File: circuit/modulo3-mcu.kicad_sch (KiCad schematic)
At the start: 46 parts, among them Q1 BS250, Q2 BS170, U1 74LVC2G32DC, U10 PWR_CONN, U11 FOOTSWITCH, U2 AVR64DA64, U3 SN74LVC1G17, U4 UPDI, U5 TOUCHSCREEN_240x320, U6 FV1_CONN, U7 DBG_UART, U8 AMPCTRL, Y1 32768Hz

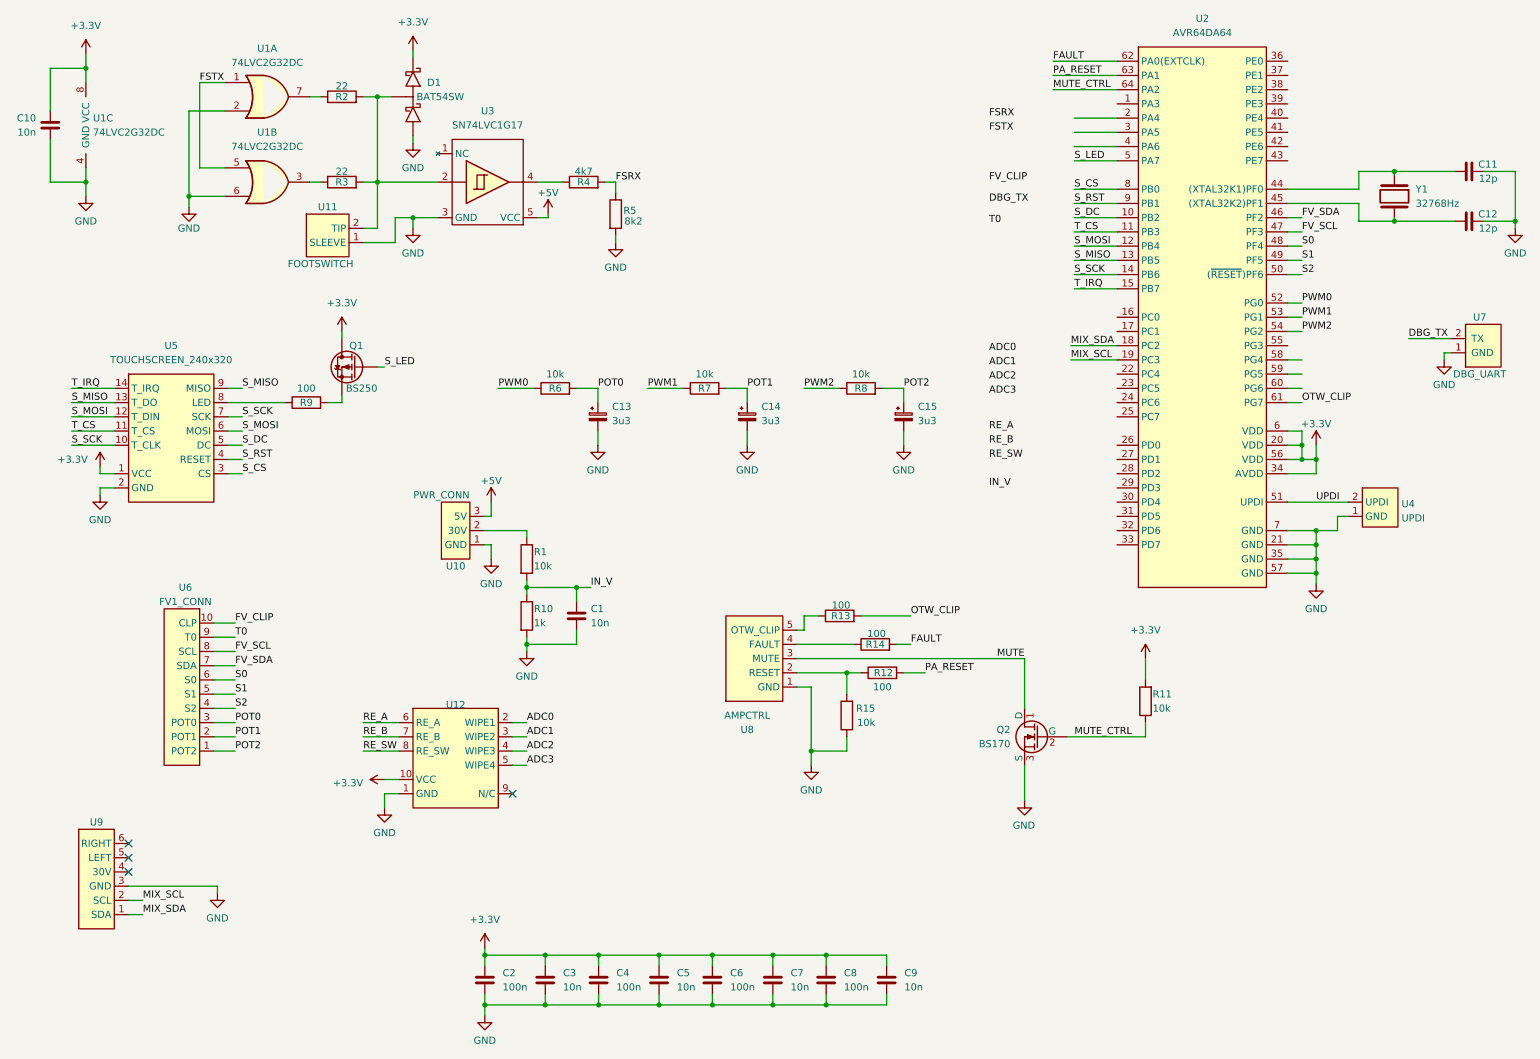
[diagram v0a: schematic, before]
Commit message: mcu pcb first draft done!
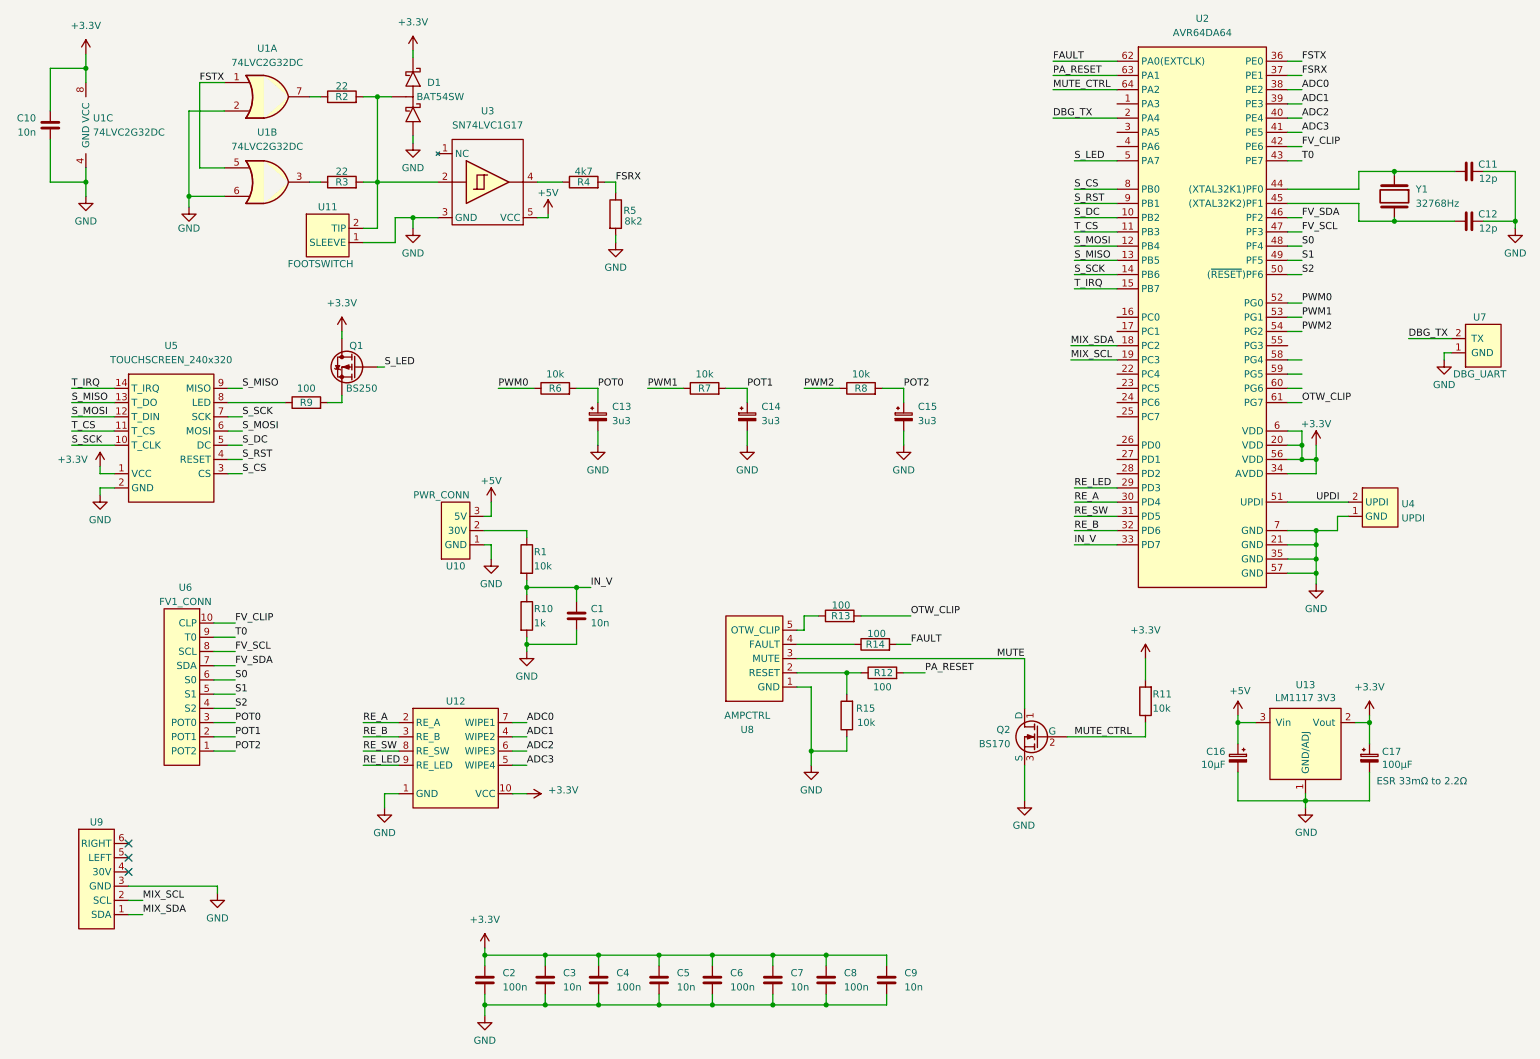
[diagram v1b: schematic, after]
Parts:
- added C16: 10µF, myAmp:CPOL_D4_P1.5, symbol myAmp:CPOL
- added C17: 100µF, myAmp:CPOL_D6.3_P2.5, symbol myAmp:CPOL
- added U13: LM1117 3V3, myAmp:SOT-223, symbol myAmp:LM1117
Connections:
- net +3.3V: now also C17.1, U13.2 (Vout)
- net +5V: now also C16.1, U13.3 (Vin)
- net ADC0: now also U12.7 (WIPE1), U2.38 (PE2); no longer U12.2 (WIPE1)
- net ADC1: now also U12.4 (WIPE2), U2.39 (PE3); no longer U12.3 (WIPE2)
- net ADC2: now also U12.6 (WIPE3), U2.40 (PE4); no longer U12.4 (WIPE3)
- net ADC3: now also U2.41 (PE5)
- net DBG_TX: now also U2.2 (PA4)
- net FSRX: now also U2.37 (PE1)
- net FSTX: now also U2.36 (PE0)
- net FV_CLIP: now also U2.42 (PE6)
- net GND: now also C16.2, C17.2, U13.1 (GND/ADJ)
- net IN_V: now also U2.33 (PD7)
- net RE_A: now also U12.2 (RE_A), U2.30 (PD4); no longer U12.6 (RE_A)
- net RE_B: now also U12.3 (RE_B), U2.32 (PD6); no longer U12.7 (RE_B)
- net RE_SW: now also U2.31 (PD5)
- net T0: now also U2.43 (PE7)
- net RE_LED: now reaches U2.29 (PD3)
- net RE_LED: now also U12.9 (RE_LED)
- no-connect marks 4 -> 3
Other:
- note added: "ESR 33mΩ to 2.2Ω"

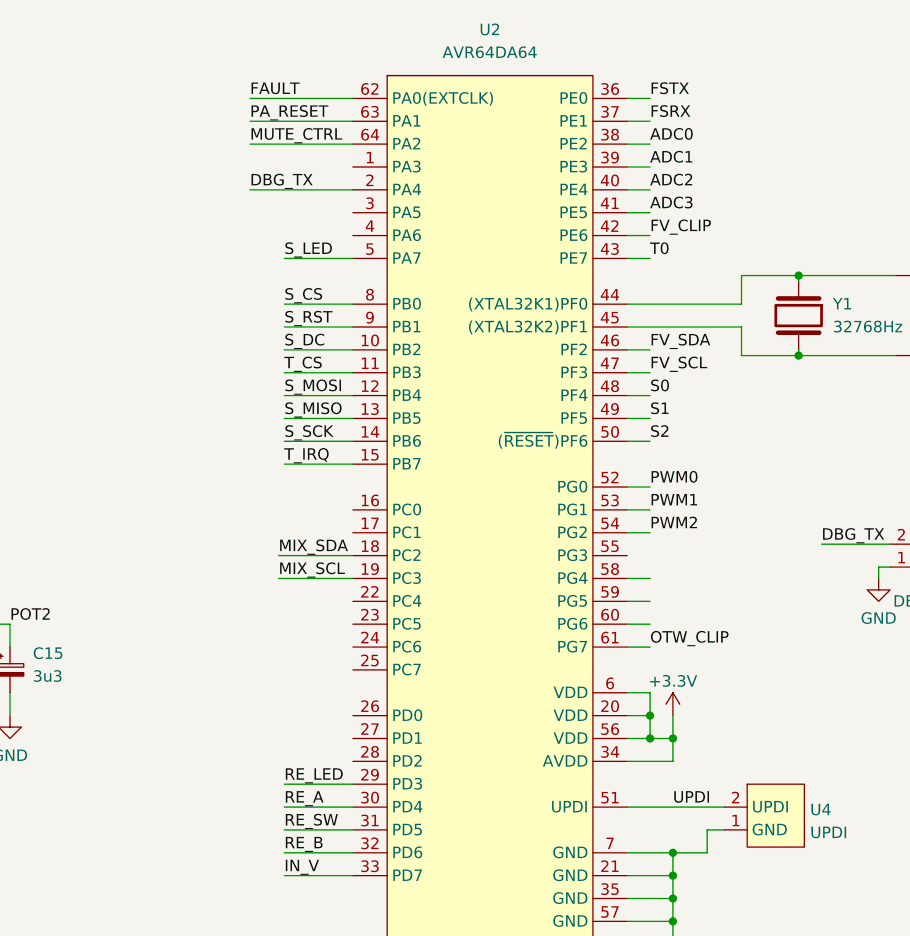
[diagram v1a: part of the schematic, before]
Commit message: added test pads for unused mcu pins
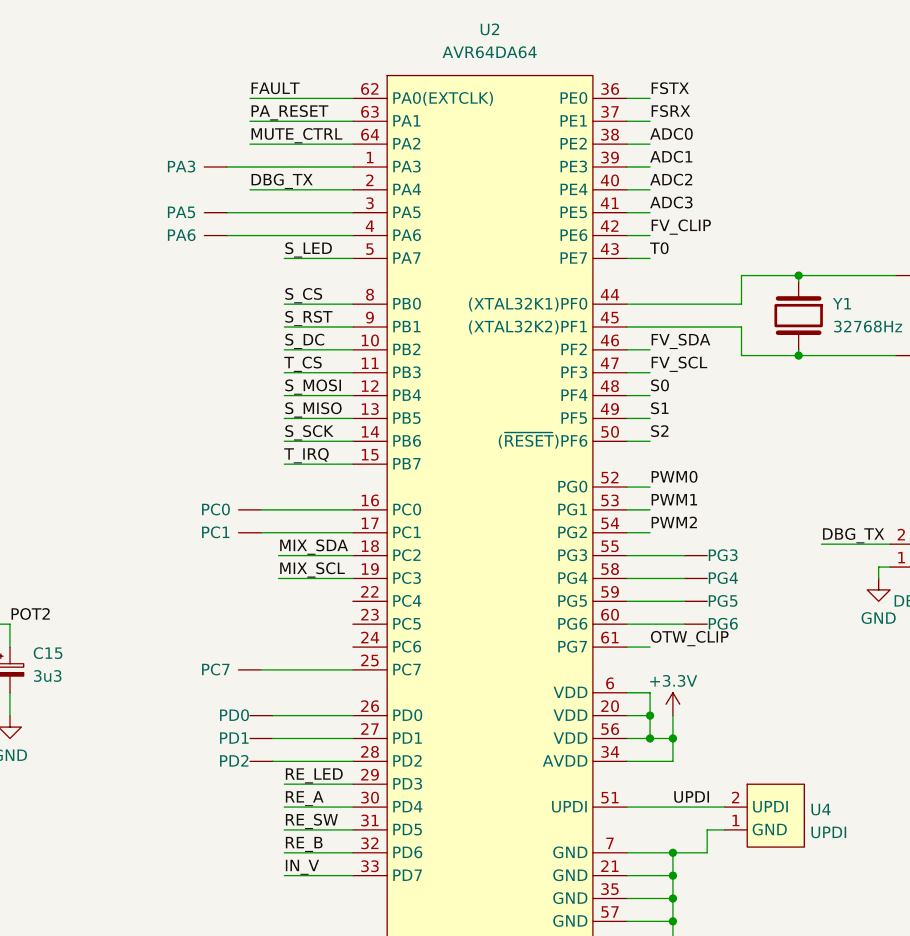
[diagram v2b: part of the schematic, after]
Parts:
- added T1: PA3, myAmp:TestPad, symbol myAmp:TEST
- added T10: PD1, myAmp:TestPad, symbol myAmp:TEST
- added T11: PD0, myAmp:TestPad, symbol myAmp:TEST
- added T12: PC7, myAmp:TestPad, symbol myAmp:TEST
- added T13: PG6, myAmp:TestPad, symbol myAmp:TEST
- added T2: PD2, myAmp:TestPad, symbol myAmp:TEST
- added T3: PA6, myAmp:TestPad, symbol myAmp:TEST
- added T4: PC0, myAmp:TestPad, symbol myAmp:TEST
- added T5: PC1, myAmp:TestPad, symbol myAmp:TEST
- added T6: PG5, myAmp:TestPad, symbol myAmp:TEST
- added T7: PG4, myAmp:TestPad, symbol myAmp:TEST
- added T8: PG3, myAmp:TestPad, symbol myAmp:TEST
- added T9: PA5, myAmp:TestPad, symbol myAmp:TEST
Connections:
- net at U2.1 (PA3): now also T1.1
- net at U2.16 (PC0): now also T4.1
- net at U2.17 (PC1): now also T5.1
- net at U2.25 (PC7): now also T12.1
- net at U2.26 (PD0): now also T11.1
- net at U2.27 (PD1): now also T10.1
- net at U2.28 (PD2): now also T2.1
- net at U2.3 (PA5): now also T9.1
- net at U2.4 (PA6): now also T3.1
- net at U2.55 (PG3): now also T8.1
- net at U2.58 (PG4): now also T7.1
- net at U2.59 (PG5): now also T6.1
- net at U2.60 (PG6): now also T13.1

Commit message: ready to panelize
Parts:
- removed U11: FOOTSWITCH, myAmp:FOOTSWITCH, symbol myAmp:FOOTSWITCH
- added T14: PC4, myAmp:TestPad, symbol myAmp:TEST
- added T15: PC5, myAmp:TestPad, symbol myAmp:TEST
- added T16: PC6, myAmp:TestPad, symbol myAmp:TEST
- added U11: FOOTSWITCH, myAmp:EXT_JACK, symbol myAmp:EXT_JACK
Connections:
- net GND: now also U11.1 (SLEEVE)
- net at D1.3, R2.2, R3.2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: now also U11.2 (TIP)
- net at U2.22 (PC4): now also T14.1
- net at U2.23 (PC5): now also T15.1
- net at U2.24 (PC6): now also T16.1
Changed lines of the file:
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@@
     (stroke (width 0) (type default))
   )
+  (wire (pts (xy 200.66 80.01) (xy 210.82 80.01))
+    (stroke (width 0) (type default))
+  )
   (wire (pts (xy 52.07 85.09) (xy 54.61 85.09))
     (stroke (width 0) (type default))
@@
     (stroke (width 0) (type default))
   )
+  (wire (pts (xy 200.66 82.55) (xy 210.82 82.55))
+    (stroke (width 0) (type default))
+  )
   (wire (pts (xy 97.917 188.214) (xy 97.917 190.119))
     (stroke (width 0) (type default))
@@
     (stroke (width 0) (type default))
   )
+  (wire (pts (xy 200.66 77.47) (xy 210.82 77.47))
+    (stroke (width 0) (type default))
+  )
   (wire (pts (xy 262.89 71.12) (xy 270.51 71.12))
     (stroke (width 0) (type default))
@@
     )
   )
-  (symbol (lib_id "myAmp:FOOTSWITCH") (at 71.12 52.705 0) (unit 1)
-    (in_bom yes) (on_board yes) (dnp no)
-    (property "Reference" "U11" (at 69.85 47.625 0)
-      (effects (font (size 1.27 1.27)))
-    )
-    (property "Value" "FOOTSWITCH" (at 68.58 57.785 0)
-      (effects (font (size 1.27 1.27)))
-    )
-    (property "Footprint" "myAmp:FOOTSWITCH" (at 76.2 52.705 0)
-      (effects (font (size 1.27 1.27)) hide)
-    )
-    (property "Datasheet" "" (at 76.2 52.705 0)
-      (effects (font (size 1.27 1.27)) hide)
-    )
-    (pin "1")
-    (pin "2")
-    (instances
-      (project "modulo3-mcu"
-        (path "/0f0bc50f-3b2c-45bf-9734-4d8155cef241"
-          (reference "U11") (unit 1)
-        )
-      )
-    )
-  )
   (symbol (lib_id "myAmp:R") (at 137.16 80.01 90) (unit 1)
     (in_bom yes) (on_board yes) (dnp no)
@@
     )
   )
+  (symbol (lib_id "myAmp:EXT_JACK") (at 71.12 52.705 0) (unit 1)
+    (in_bom yes) (on_board yes) (dnp no)
+    (property "Reference" "U11" (at 69.85 47.625 0)
+      (effects (font (size 1.27 1.27)))
+    )
+    (property "Value" "FOOTSWITCH" (at 69.85 57.785 0)
+      (effects (font (size 1.27 1.27)))
+    )
+    (property "Footprint" "myAmp:EXT_JACK" (at 71.12 57.785 0)
+      (effects (font (size 1.27 1.27)) hide)
+    )
+    (property "Datasheet" "" (at 76.2 52.705 0)
+      (effects (font (size 1.27 1.27)) hide)
+    )
+    (pin "1")
+    (pin "2")
+    (instances
+      (project "modulo3-mcu"
+        (path "/0f0bc50f-3b2c-45bf-9734-4d8155cef241"
+          (reference "U11") (unit 1)
+        )
+      )
+    )
+  )
   (symbol (lib_id "power:+3.3V") (at 72.39 69.85 0) (unit 1)
     (in_bom yes) (on_board yes) (dnp no) (fields_autoplaced)
@@
     )
   )
+  (symbol (lib_id "myAmp:TEST") (at 198.12 82.55 180) (unit 1)
+    (in_bom yes) (on_board yes) (dnp no)
+    (property "Reference" "T16" (at 198.12 78.74 0)
+      (effects (font (size 1.27 1.27)) hide)
+    )
+    (property "Value" "PC6" (at 195.58 82.55 0)
+      (effects (font (size 1.27 1.27)))
+    )
+    (property "Footprint" "myAmp:TestPad" (at 198.12 82.55 0)
+      (effects (font (size 1.27 1.27)) hide)
+    )
+    (property "Datasheet" "" (at 198.12 82.55 0)
+      (effects (font (size 1.27 1.27)) hide)
+    )
+    (pin "1")
+    (instances
+      (project "modulo3-mcu"
+        (path "/0f0bc50f-3b2c-45bf-9734-4d8155cef241"
+          (reference "T16") (unit 1)
+        )
+      )
+    )
+  )
   (symbol (lib_id "myAmp:SN74LVC1G17") (at 98.425 43.18 0) (unit 1)
     (in_bom yes) (on_board yes) (dnp no) (fields_autoplaced)
@@
     )
   )
+  (symbol (lib_id "myAmp:TEST") (at 198.12 80.01 180) (unit 1)
+    (in_bom yes) (on_board yes) (dnp no)
+    (property "Reference" "T15" (at 198.12 76.2 0)
+      (effects (font (size 1.27 1.27)) hide)
+    )
+    (property "Value" "PC5" (at 195.58 80.01 0)
+      (effects (font (size 1.27 1.27)))
+    )
+    (property "Footprint" "myAmp:TestPad" (at 198.12 80.01 0)
+      (effects (font (size 1.27 1.27)) hide)
+    )
+    (property "Datasheet" "" (at 198.12 80.01 0)
+      (effects (font (size 1.27 1.27)) hide)
+    )
+    (pin "1")
+    (instances
+      (project "modulo3-mcu"
+        (path "/0f0bc50f-3b2c-45bf-9734-4d8155cef241"
+          (reference "T15") (unit 1)
+        )
+      )
+    )
+  )
   (symbol (lib_id "power:GND") (at 156.21 147.32 0) (unit 1)
     (in_bom yes) (on_board yes) (dnp no) (fields_autoplaced)
@@
         )
       )
+    )
+  )
+  (symbol (lib_id "myAmp:TEST") (at 198.12 77.47 180) (unit 1)
+    (in_bom yes) (on_board yes) (dnp no)
+    (property "Reference" "T14" (at 198.12 73.66 0)
+      (effects (font (size 1.27 1.27)) hide)
+    )
+    (property "Value" "PC4" (at 195.58 77.47 0)
+      (effects (font (size 1.27 1.27)))
+    )
+    (property "Footprint" "myAmp:TestPad" (at 198.12 77.47 0)
+      (effects (font (size 1.27 1.27)) hide)
+    )
+    (property "Datasheet" "" (at 198.12 77.47 0)
+      (effects (font (size 1.27 1.27)) hide)
+    )
+    (pin "1")
+    (instances
+      (project "modulo3-mcu"
+        (path "/0f0bc50f-3b2c-45bf-9734-4d8155cef241"
+          (reference "T14") (unit 1)
+        )
+      )

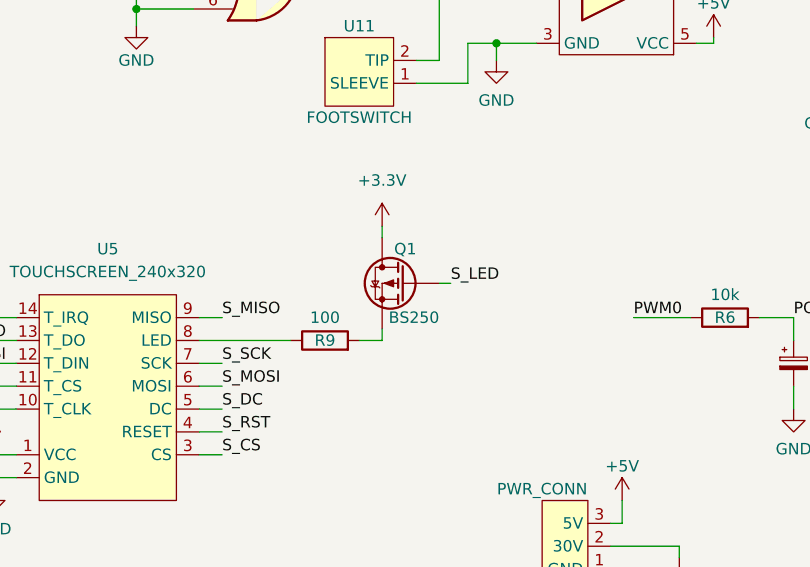
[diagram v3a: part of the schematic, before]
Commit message: fixed p mosfet for screen LED; started src
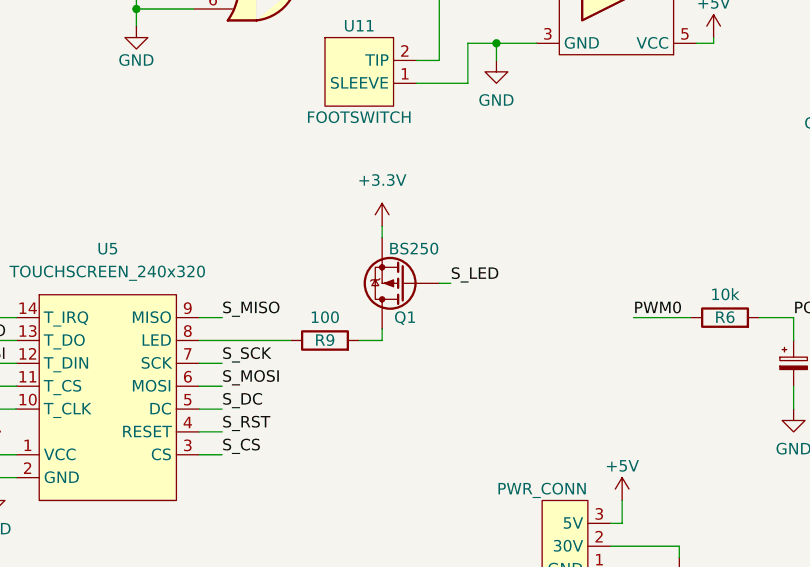
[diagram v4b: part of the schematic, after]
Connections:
- net +3.3V: now also Q1.3 (S); no longer Q1.1 (D)
- net at R9.2: now also Q1.1 (D); no longer Q1.3 (S)
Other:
- moved on the sheet: Q1
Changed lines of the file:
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@@
     )
   )
-  (symbol (lib_id "myAmp:BS250") (at 74.93 76.2 0) (mirror y) (unit 1)
+  (symbol (lib_id "myAmp:BS250") (at 74.93 76.2 180) (unit 1)
     (in_bom yes) (on_board yes) (dnp no)
-    (property "Reference" "Q1" (at 76.2 72.39 0)
+    (property "Reference" "Q1" (at 76.2 80.01 0)
       (effects (font (size 1.27 1.27)) (justify left))
     )
-    (property "Value" "BS250" (at 78.74 80.01 0)
+    (property "Value" "BS250" (at 78.74 72.39 0)
       (effects (font (size 1.27 1.27)) (justify left))
     )
-    (property "Footprint" "myAmp:TO-92_Inline_Wide" (at 69.85 73.66 0)
+    (property "Footprint" "myAmp:TO-92_Inline_Wide" (at 69.85 78.74 0)
       (effects (font (size 1.27 1.27)) hide)
     )
